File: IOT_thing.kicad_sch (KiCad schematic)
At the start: 26 parts, among them J1 USB_C_Receptacle_USB2.0_16P, J2 Conn_01x04, J3 Screw_Terminal_01x03, J4 Screw_Terminal_01x08, J5 Screw_Terminal_01x02, K1 RT314A05, Q1 UMH3N, Q2 UMH3N, Q3 BC817, SW1 SW_SPST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

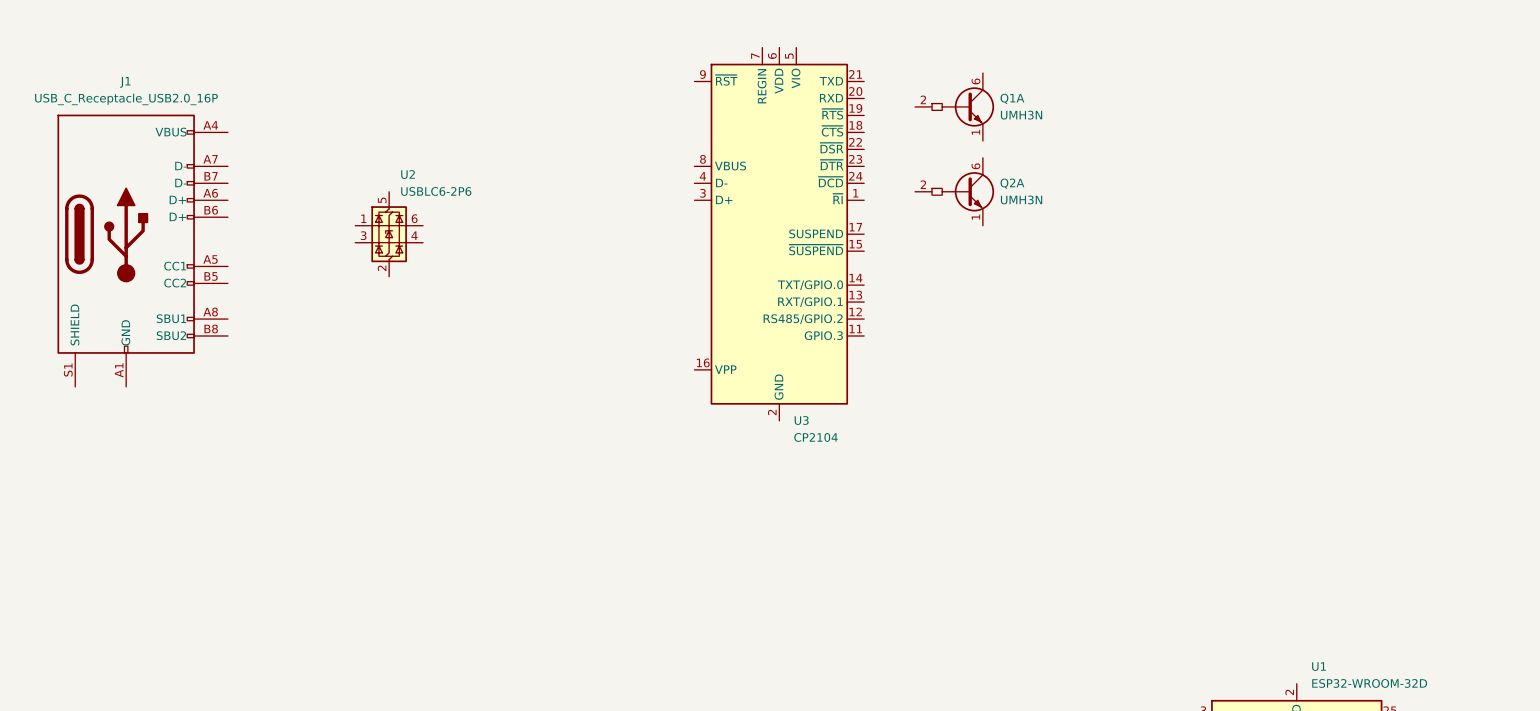
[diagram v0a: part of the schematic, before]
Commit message: Finished wiring the programming interface
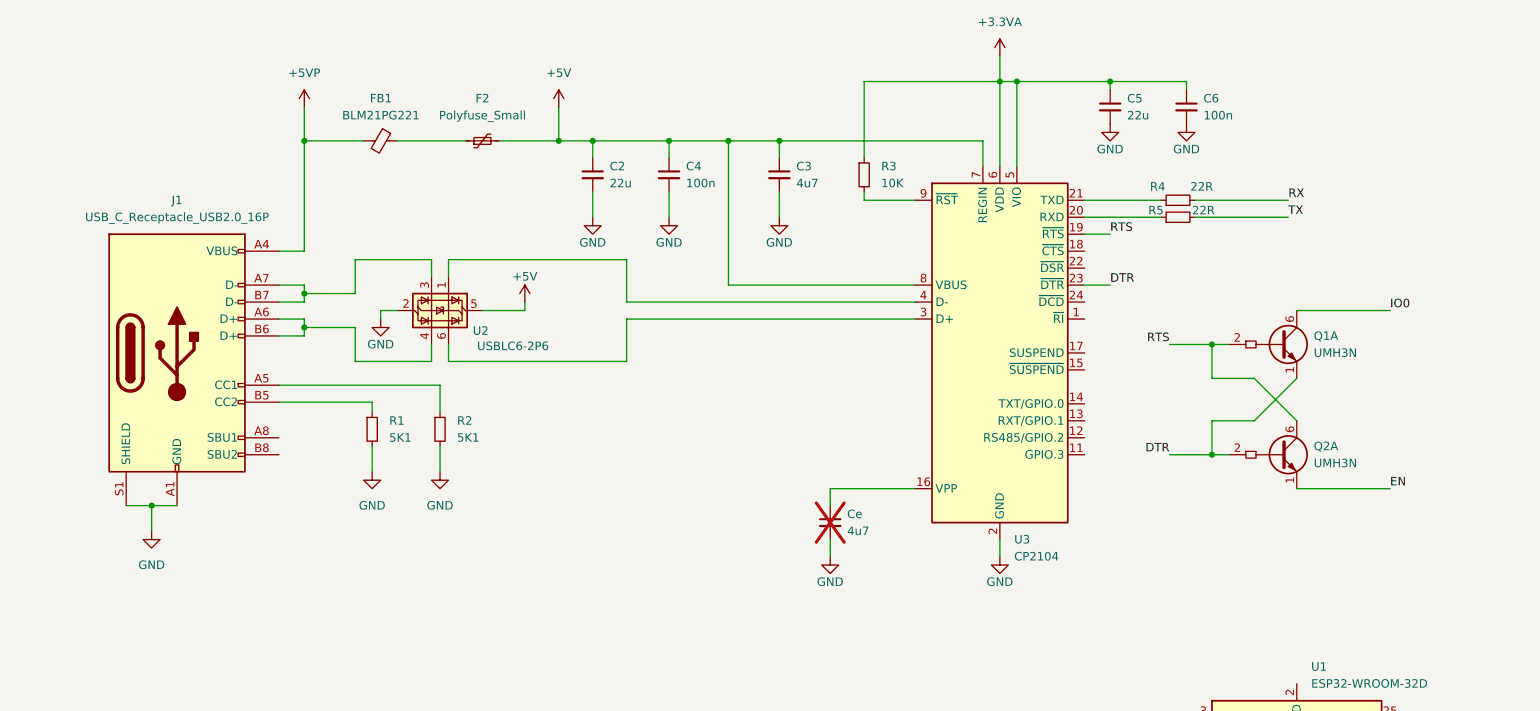
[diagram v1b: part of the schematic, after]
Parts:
- added C2, C5: 22u, symbol Device:C_Small
- added C3, Ce: 4u7, symbol Device:C_Small
- added C4, C6: 100n, symbol Device:C_Small
- added F2: Polyfuse_Small, symbol Device:Polyfuse_Small
- added FB1: BLM21PG221, symbol Device:FerriteBead_Small
- added R1, R2: 5K1, symbol Device:R_Small
- added R3: 10K, symbol Device:R_Small
- added R4, R5: 22R, symbol Device:R_Small
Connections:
- net DTR: now reaches Q1.1 (E1)
- net DTR: now also Q2.2 (B1), U3.23 (~{DTR})
- net RTS: now reaches Q1.2 (B1)
- net RTS: now also Q2.6 (C1), U3.19 (~{RTS})
- net IO0: now reaches Q1.6 (C1)
- net GND: now reaches J1.A1 (GND), J1.A12 (GND), J1.B1 (GND), J1.B12 (GND)
- net GND: now also J1.S1 (SHIELD), U2.2 (GND), U3.2 (GND), U3.25 (GND), C2.2, C3.2, C4.2, C5.2, C6.2, Ce.2, R1.2, R2.2
- net +5VP: now reaches J1.A4 (VBUS), J1.A9 (VBUS), J1.B4 (VBUS), J1.B9 (VBUS)
- net +5VP: now also FB1.2
- net at J1.A5 (CC1): now also R2.1
- net at J1.A6 (D+): now also J1.B6 (D+), U2.4 (I/O2)
- net at J1.A7 (D-): now also J1.B7 (D-), U2.3 (I/O2)
- net at J1.B5 (CC2): now also R1.1
- net at U3.16 (VPP): now also Ce.1
- net at U3.20 (RXD): now also R5.1
- net at U3.21 (TXD): now also R4.1
- net at U3.3 (D+): now also U2.6 (I/O1)
- net at U3.4 (D-): now also U2.1 (I/O1)
- net +3.3VA: now reaches U3.5 (VIO)
- net +3.3VA: now also U3.6 (VDD), C5.1, C6.1, R3.1
- net +5V: now reaches U3.7 (REGIN)
- net +5V: now also U2.5 (VBUS), U3.8 (VBUS), C2.1, C3.1, C4.1, F2.2
- net at U3.9 (~{RST}): now also R3.2
- net EN: now reaches Q2.1 (E1)
- new net: F2.1, FB1.1
- new net RX: R4.2
- new net TX: R5.2
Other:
- moved on the sheet: Q1A, Q2A, U2, U3

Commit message: Finished the power supply
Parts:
- added C7, C8: 22u, symbol Device:C_Small
- added C9: 100n, symbol Device:C_Small
- added R10, R6, R7, R9: 1K, symbol Device:R_Small
- added R8: 10K, symbol Device:R_Small
- R1, R2: value 5K1 -> 5K
- U6: value LM1117MP-3.3 -> TLV117LV-3.3V
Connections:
- net +5V: now also U6.3 (VI), C7.1
- net GND: now also D4.1 (K), H1.1, H2.1, H3.1, H4.1, SW1.1 (A), U6.1 (GND), C7.2, C8.2, C9.2
- net at D4.2 (A): now also R6.2
- net +3.3V: now reaches U6.2 (VO)
- net +3.3V: now also D3.4 (A), C8.1, R6.1, R8.1
- net SW: now reaches SW1.2 (B)
- net SW: now also C9.1, R8.2
- net at D3.1 (RK): now also R7.2
- net at D3.2 (GK): now also R9.2
- net at D3.3 (BK): now also R10.2
- new net RED_B: R10.1
- new net RED_G: R9.1
- new net RED_R: R7.1
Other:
- moved on the sheet: D3, D4, H1, H2, H3, H4, SW1, U6

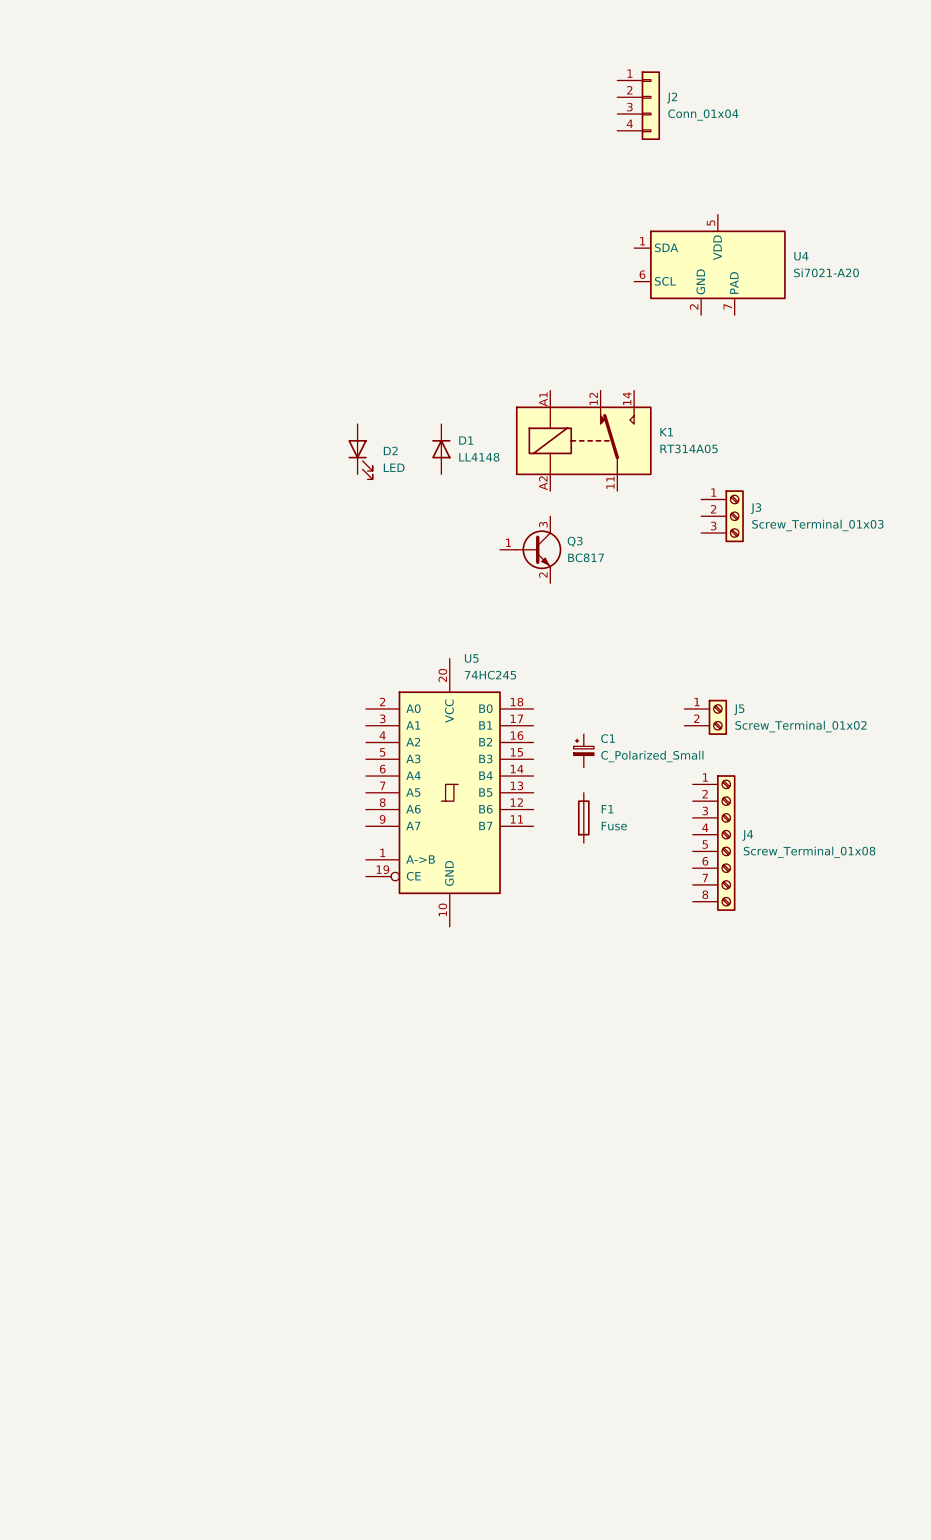
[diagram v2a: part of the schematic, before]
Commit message: Finished wiring the I2C part
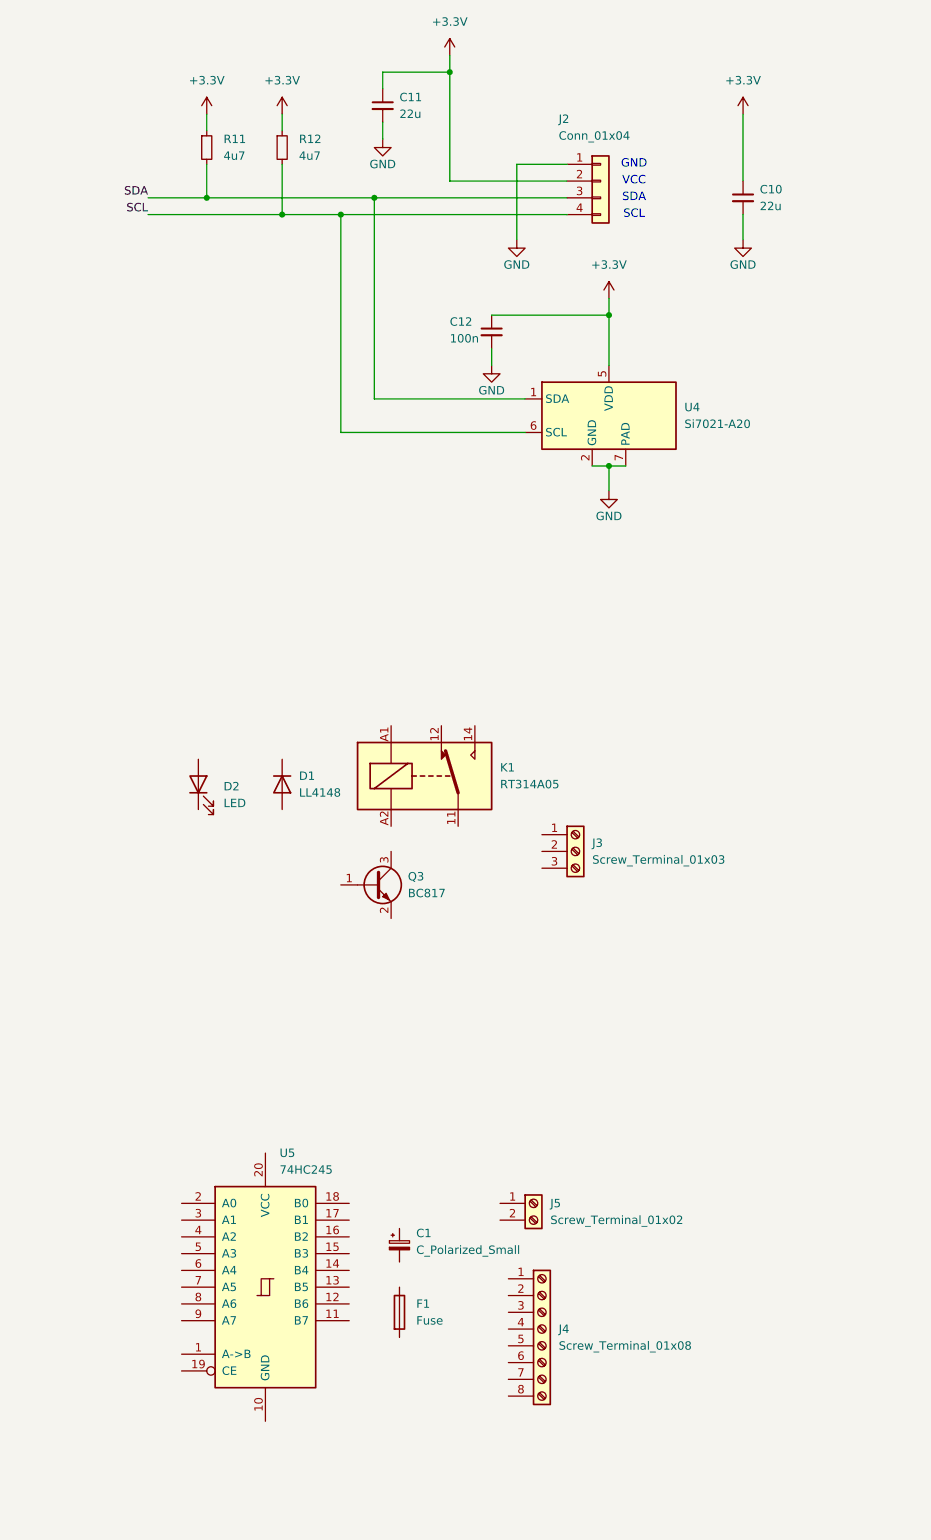
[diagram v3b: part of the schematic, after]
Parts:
- added C10, C11: 22u, symbol Device:C_Small
- added C12: 100n, symbol Device:C_Small
- added R11, R12: 4u7, symbol Device:R_Small
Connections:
- net +3.3V: now also J2.2 (Pin_2), U4.5 (VDD), C10.1, C11.1, C12.1, R11.1, R12.1
- net GND: now also J2.1 (Pin_1), U4.2 (GND), U4.7 (PAD), C10.2, C11.2, C12.2
- net SDA: now reaches U4.1 (SDA)
- net SDA: now also J2.3 (Pin_3), R11.2
- net SCL: now reaches U4.6 (SCL)
- net SCL: now also J2.4 (Pin_4), R12.2
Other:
- note added: "GND"
- note added: "SCL"
- note added: "SDA"
- note added: "VCC"
- moved on the sheet: C1, D1, D2, F1, J2, J3, J4, J5, K1, Q3, U4, U5

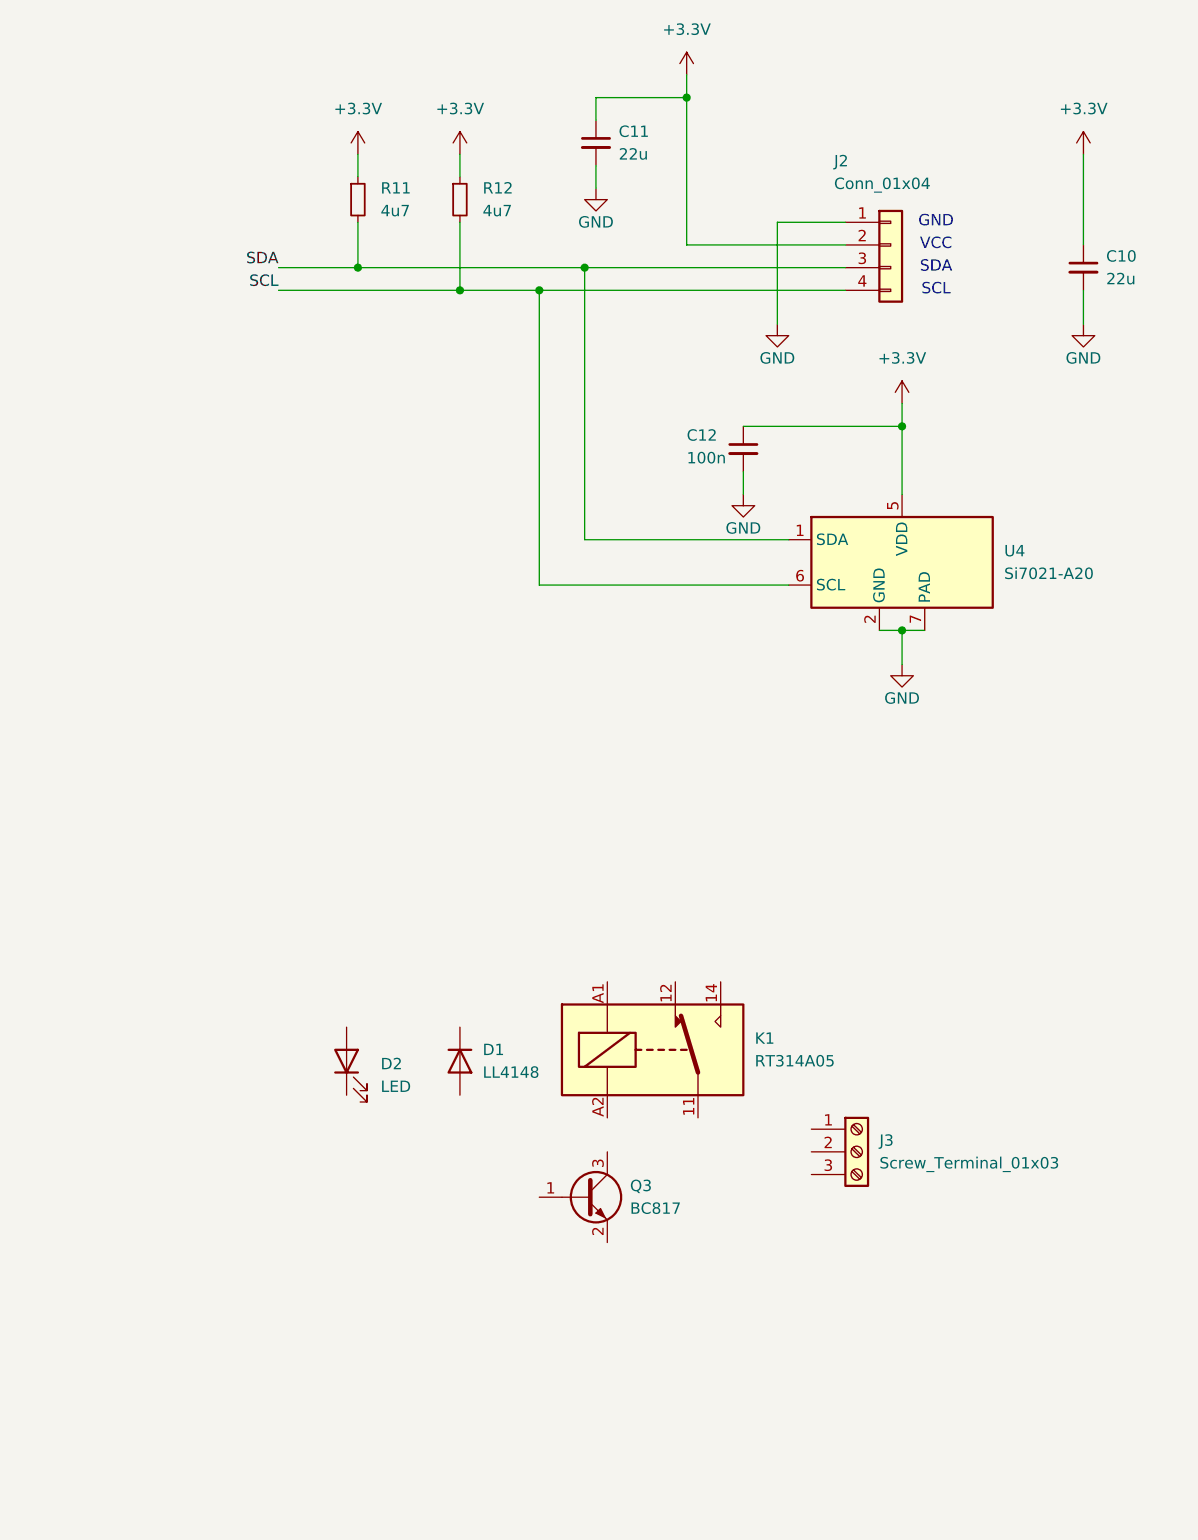
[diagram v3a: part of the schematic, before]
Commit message: Finished wiring the relay module
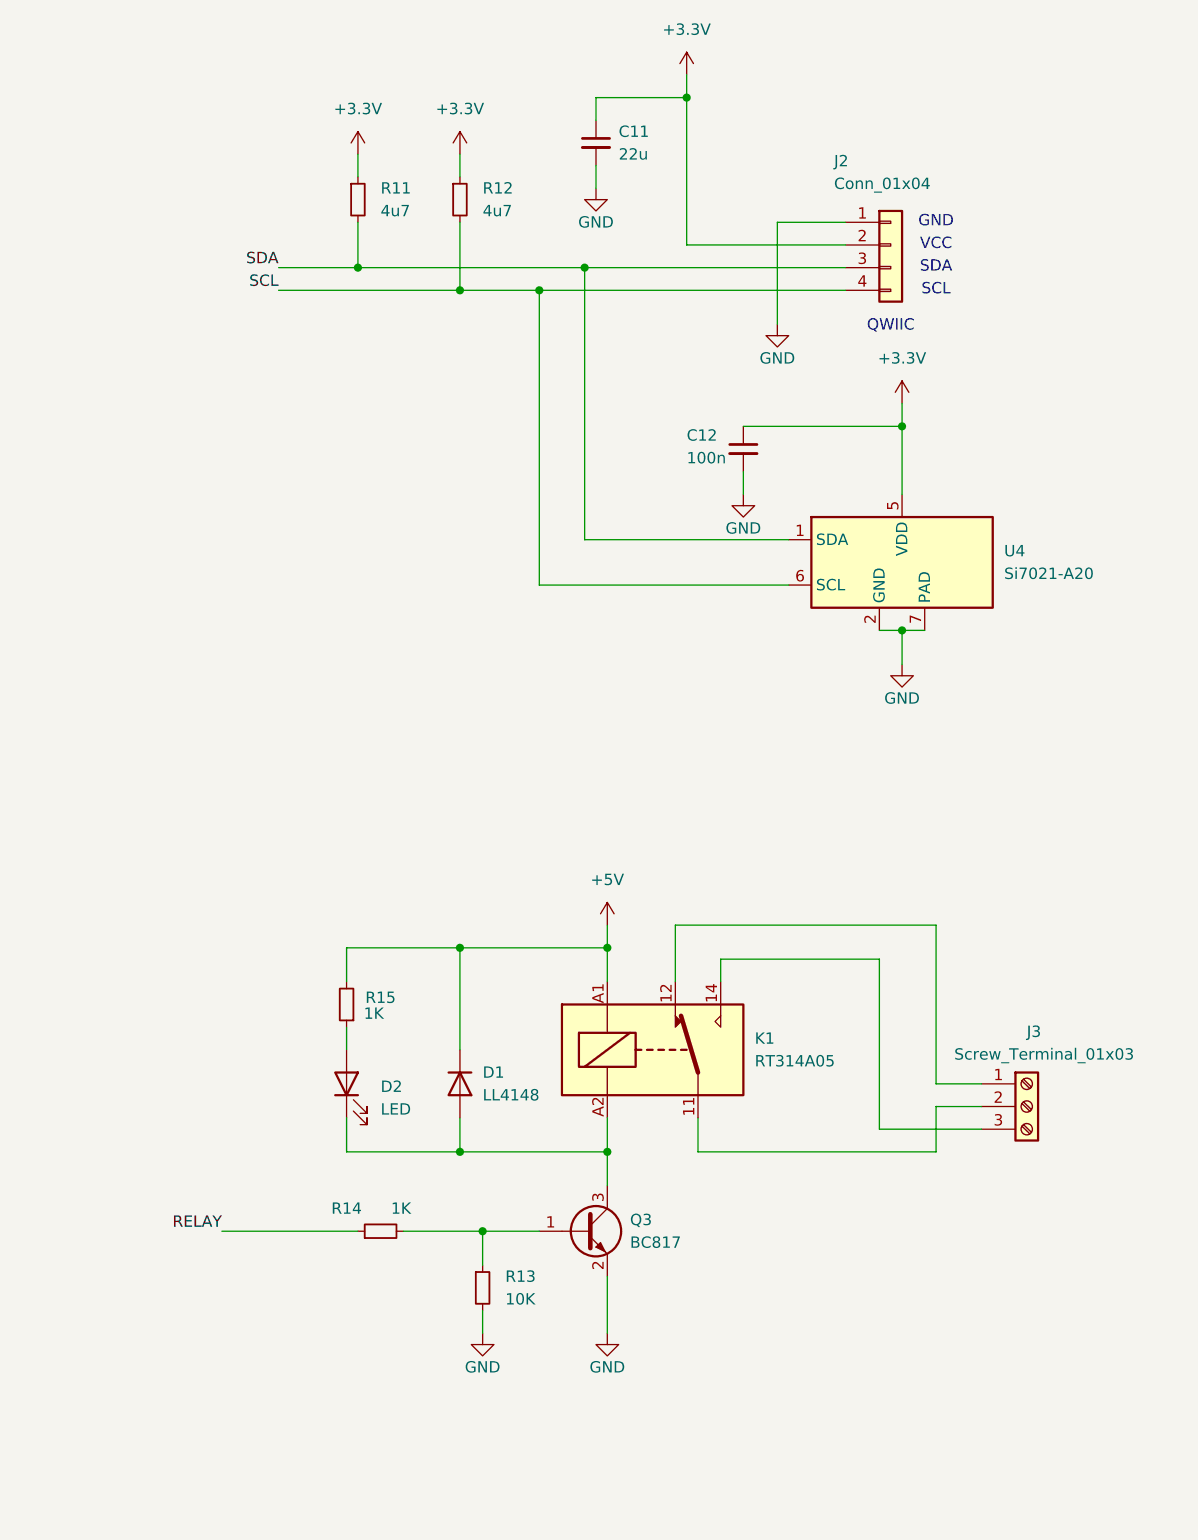
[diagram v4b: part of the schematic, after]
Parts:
- removed C10: 22u, symbol Device:C_Small
- added R13: 10K, symbol Device:R_Small
- added R14, R15: 1K, symbol Device:R_Small
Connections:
- net +5V: now also D1.1 (K), K1.A1, R15.2
- net GND: now also Q3.2 (E), R13.2
- net at J3.1 (Pin_1): now also K1.12
- net at J3.2 (Pin_2): now also K1.11
- net at J3.3 (Pin_3): now also K1.14
- net at D1.2 (A): now also D2.1 (K), K1.A2, Q3.3 (C)
- net at D2.2 (A): now also R15.1
- net at Q3.1 (B): now also R13.1, R14.2
- new net RELAY: R14.1
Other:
- note added: "QWIIC"
- moved on the sheet: D1, D2, J3, Q3
